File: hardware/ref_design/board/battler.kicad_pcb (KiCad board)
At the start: 2 copper layers, 73.4 x 151.6 mm, 171 parts, among them J1 TYPE-C-31-M-12, J2 53261-0271, J3 FH12-50S-0.5SH(55), J4 53261-0271, J5 SWD, J7 DEBUG PADS, Q1 2N7002, Q3 2N7002, Q5 AO3400A, Q6 AO3400A, Q7 2N7002, SW1 P1 UP, SW10 P2 DOWN, SW11 P2 LEFT, SW12 P2 RIGHT, SW13 P2 A, SW14 P2 B, SW15 P2 X, SW16 P2 Y, SW18 BOOTSEL, SW19 RESET, SW2 P1 DOWN, SW20 P1 SELECT, SW21 P1 START / PWR, SW22 P2 SELECT, SW23 P2 START / PWR, SW3 P1 LEFT, SW4 P1 RIGHT, SW5 P1 A, SW6 P1 B, SW7 P1 X, SW8 P1 Y, SW9 P2 UP, U1 SRV05-4, U2 BQ24073RGTR, U3 RT9013-33GB, U4 RP2354B, U6 MCP6002, U7 FM8002A, U8 SN74HC165PWR, U9 SN74HC165PWR, X1 12MHz

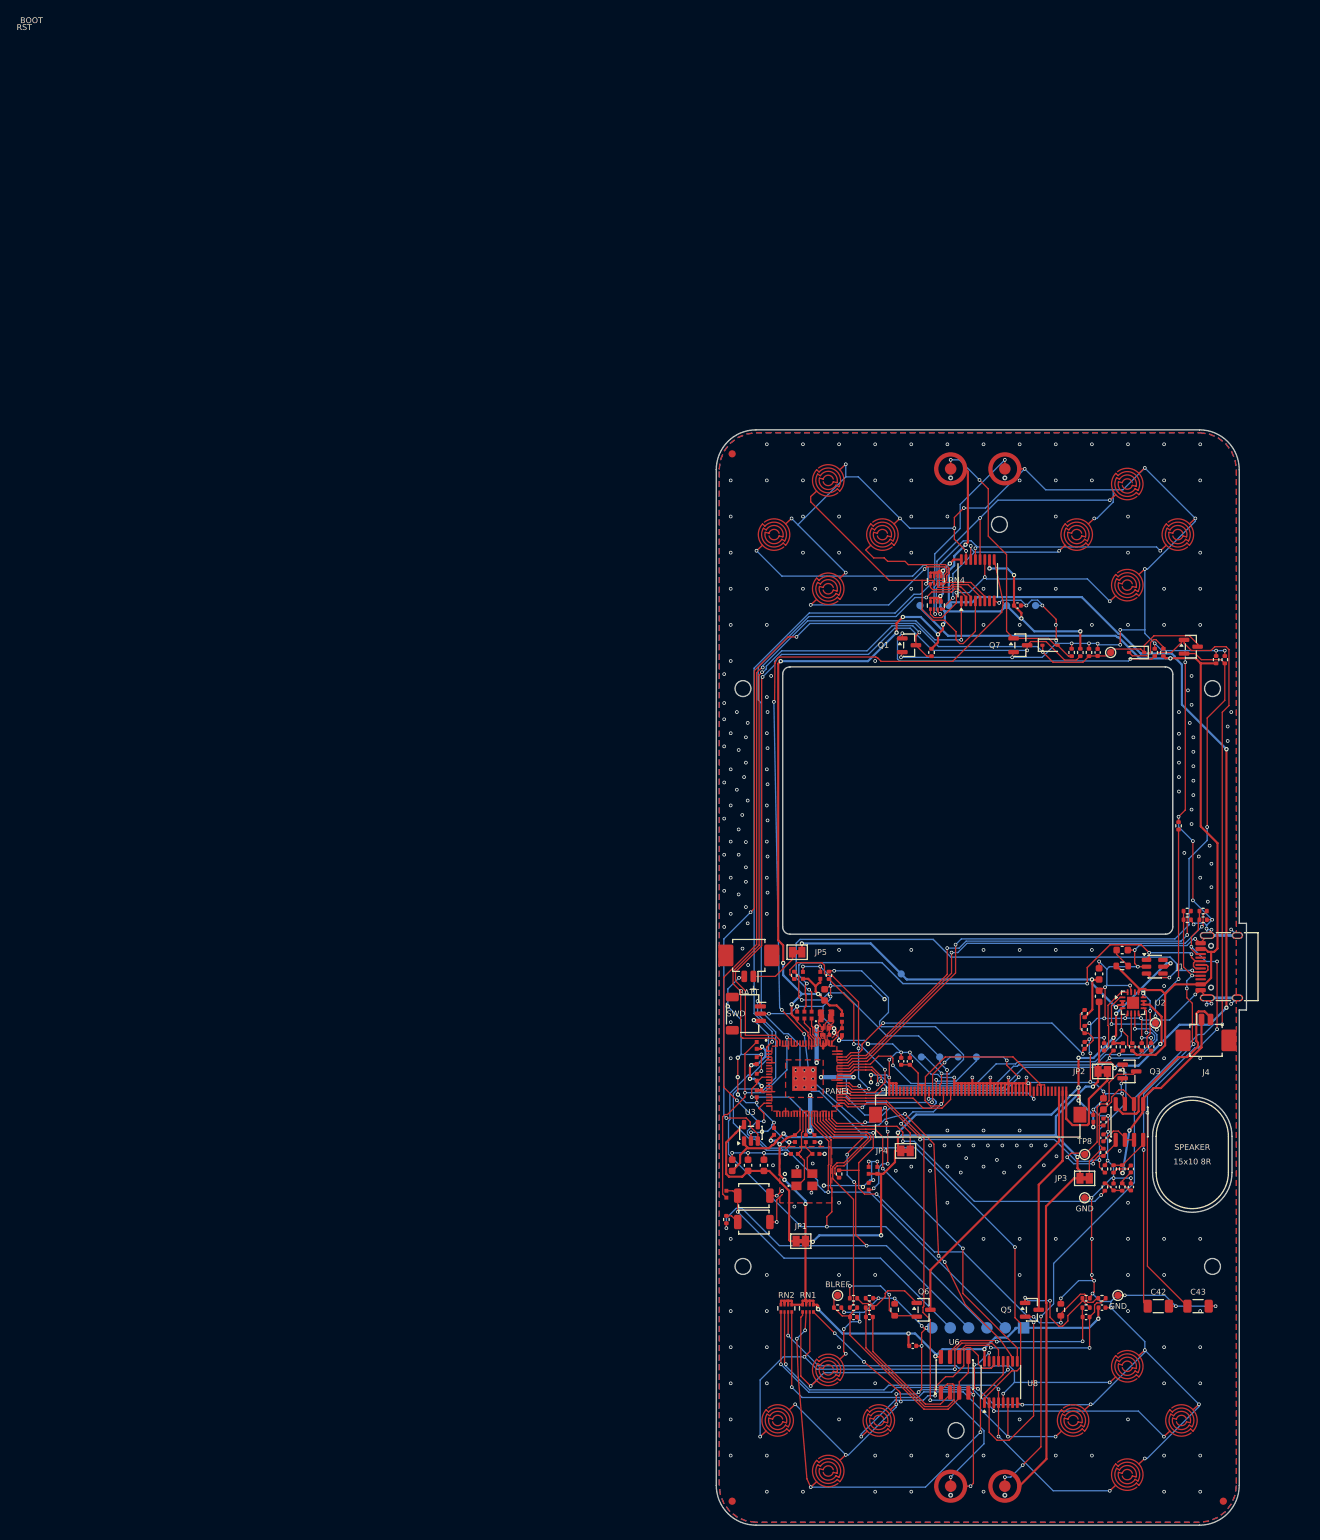
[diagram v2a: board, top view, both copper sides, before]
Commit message: ref_design: routed board for the turned cell hole (0 DRC errors, 2 connections still open: PWR_BTN_RAW and J3 pad 8's GND link), silk name on the back clear of holes, J2 nudged 0.15 in, Q1 0.15 up, pour edge clearance 0.31, docs for the V&V round 3 parts
Co-Authored-By: Claude Sonnet 5.5 <noreply@anthropic.com>
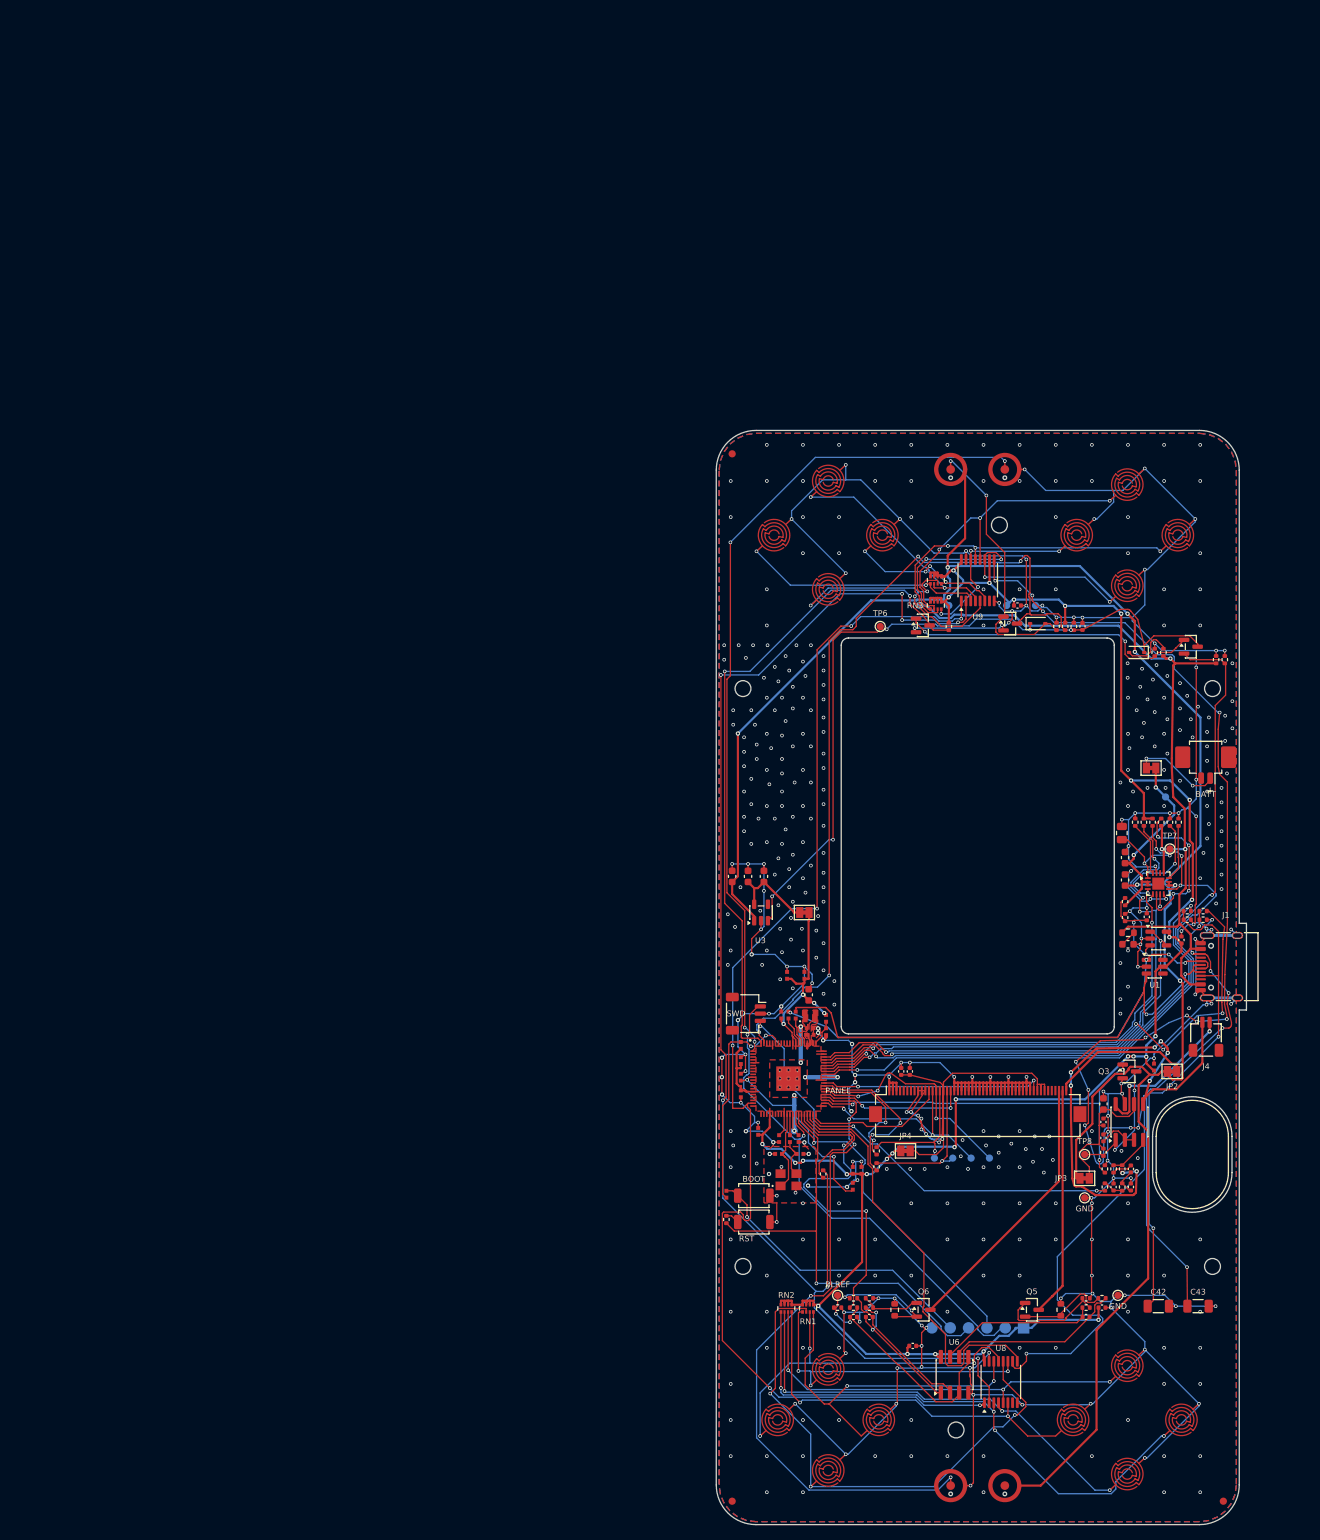
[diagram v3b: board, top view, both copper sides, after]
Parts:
- added C54: 100n, Capacitor_SMD:C_0402_1005Metric, F.Cu at (128.2, 94.8)
- added U10: MCP6001, Package_TO_SOT_SMD:SOT-23-5, F.Cu at (125.0, 94.6)
- J4: value 53261-0271 -> SM02B-SRSS-TB; footprint Connector_Molex:Molex_PicoBlade_53261-0271_1x02-1MP_P1.25mm_Horizontal -> Connector_JST:JST_SH_SM02B-SRSS-TB_1x02-1MP_P1.00mm_Horizontal
- R14, RN1, RN2, RN3, RN4: value 10k -> 47k
- R43: value 100k -> 220k
- R61: value 3.9k -> 3.74k
- TH1: value 10k B3950 -> 10k B4460; footprint Resistor_SMD:R_0402_1005Metric -> Resistor_SMD:R_0805_2012Metric
- moved J2 68.9 mm to (131.5, 70.0)
- moved JP5 55.2 mm to (124.0, 71.0)
- moved JP1 45.5 mm to (76.0, 91.0)
- moved TP3 44.0 mm to (126.0, 75.0)
- moved C5 40.0 mm to (66.0, 86.0)
- moved C6 40.0 mm to (68.2, 86.0)
- moved C7 40.0 mm to (70.4, 86.0)
- moved TP6 32.1 mm to (86.5, 51.4)
- moved R5 31.4 mm to (121.8, 78.5)
- moved R9 31.4 mm to (123.0, 78.5)
- moved R10 31.4 mm to (124.2, 78.5)
- moved R43 31.4 mm to (125.4, 78.5)
- moved R44 31.3 mm to (126.6, 78.5)
- moved R64 31.3 mm to (127.8, 78.5)
- moved U3 30.5 mm to (70.0, 91.0)
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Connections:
- C8 pad 1: VBAT_SENSE -> /Power/VBAT_DIV
- R17 pad 2: VBAT_SENSE -> /Power/VBAT_DIV
- R18 pad 1: VBAT_SENSE -> /Power/VBAT_DIV
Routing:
- net PWR_BTN_RAW: track 183.4 -> 41.7 mm, vias 6 -> 2
- net /Audio/SPK_P: track 26.0 -> 70.4 mm, vias 2 -> 8
- net /Buttons/SR_CHAIN: track 157.0 -> 197.1 mm, vias 6 -> 14
- net /Power/PWR_EN: track 141.1 -> 103.3 mm, vias 4 -> 5
- net CHG_STAT_N: track 55.4 -> 91.0 mm, vias 3 -> 4
- net VBAT: track 57.0 -> 26.4 mm, vias 3 -> 2
- net CHG_PG_N: track 56.0 -> 84.5 mm, vias 3 -> 5
- net CHG_OFF: track 53.1 -> 81.3 mm, vias 2 -> 4
- net /USB_Charger/CHG_TEMP: track 40.2 -> 12.1 mm, vias 4 -> 2
- net VSYS: track 260.5 -> 288.3 mm, vias 8 -> 7
- net /Display/LCD_3V3: track 48.6 -> 75.3 mm, vias 2 -> 8
- net P1_SELECT: track 69.5 -> 91.5 mm, vias 2 -> 4
- net SWDIO: track 85.6 -> 63.9 mm
- net /Display/LCD_SCK: track 38.3 -> 18.0 mm, vias 2 -> 1
- net +3V3: track 358.6 -> 340.8 mm, vias 38 -> 32
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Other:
- board size 73.4 x 151.6 mm -> 73.4 x 151.5 mm
- board text removed: "15x10 8R"
- board text removed: "SPEAKER"

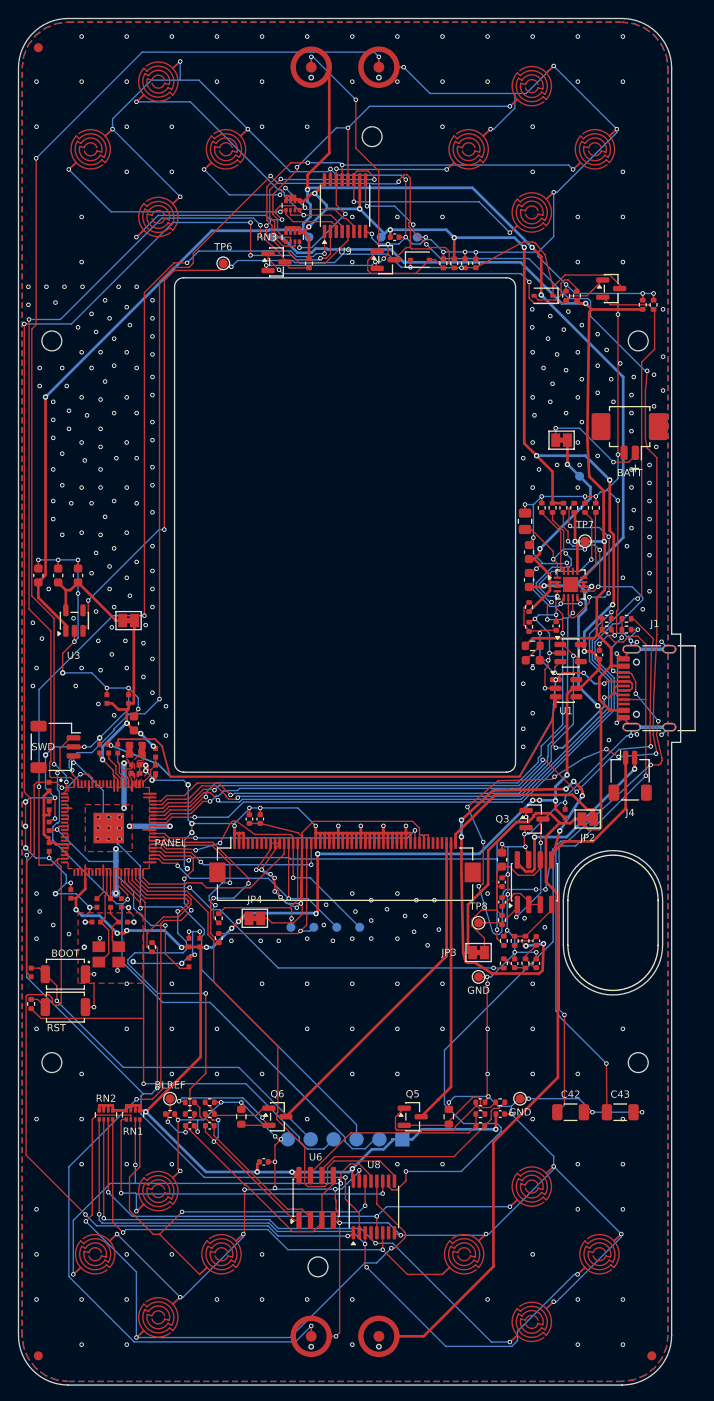
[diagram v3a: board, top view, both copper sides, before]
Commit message: ref_design: cell hole 1 mm towards seat 2 (case.scad cell_dy 1, J2 0.3 up), the latch and the seat-2 Start's row placed again, routed board with 0 unconnected and 0 DRC errors (place_search.py route, seed 32 of 20 to 55, 5627 mm); check_pcb, check_fit and the case checks pass
Co-Authored-By: Claude Sonnet 5.5 <noreply@anthropic.com>
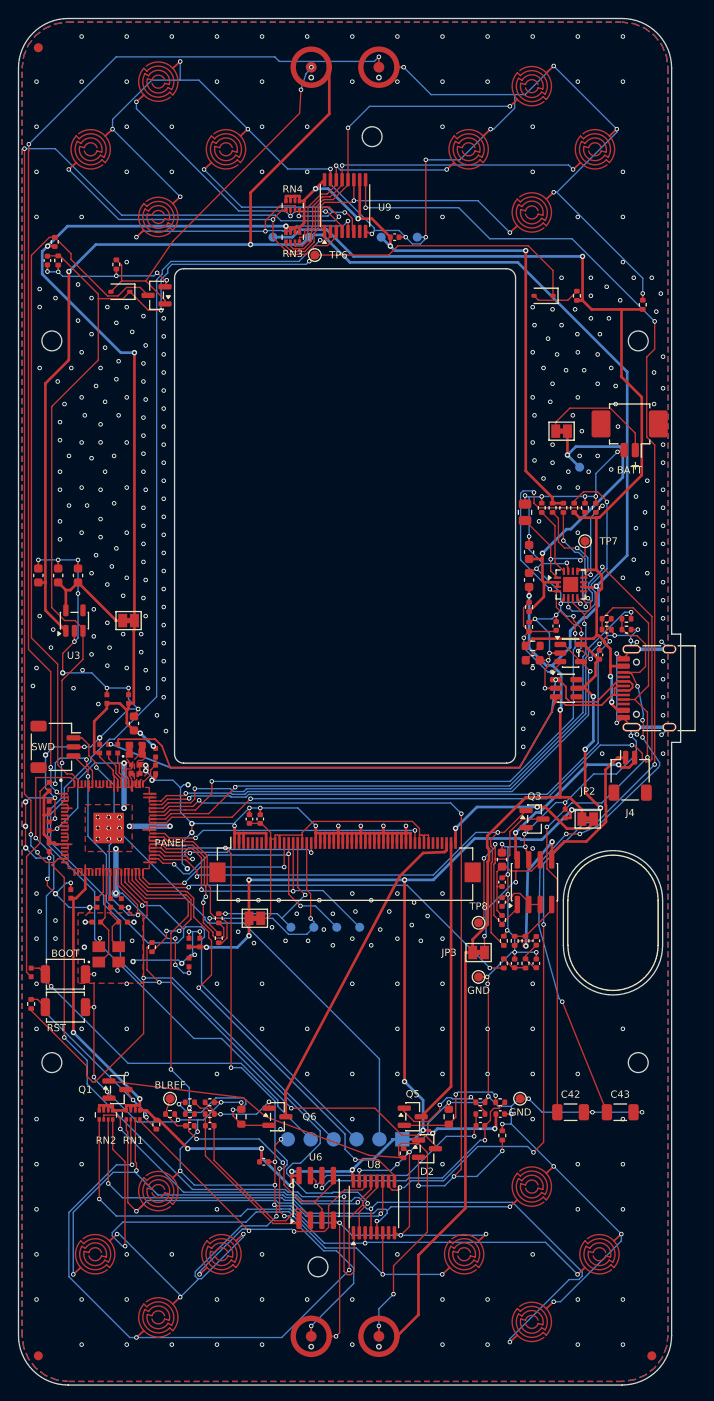
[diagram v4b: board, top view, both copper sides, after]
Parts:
- moved D2 97.5 mm to (109.1, 149.5)
- moved R16 97.0 mm to (79.1, 146.9)
- moved R13 96.7 mm to (106.5, 150.0)
- moved R42 93.6 mm to (117.4, 148.1)
- moved Q1 93.4 mm to (74.8, 143.0)
- moved C47 47.5 mm to (67.0, 51.1), turned to -90 degrees
- moved R15 45.1 mm to (68.2, 51.1), turned to -90 degrees
- moved R63 44.3 mm to (67.8, 49.0), turned to -90 degrees
- moved R62 36.3 mm to (74.6, 51.5), turned to -90 degrees
- moved D8 33.4 mm to (75.1, 54.5), turned to 180 degrees
- moved Q7 25.7 mm to (79.1, 54.9), turned to 180 degrees
- moved TP6 10.2 mm to (96.6, 50.5), turned to 180 degrees
- moved JP5 1.00 mm to (124.0, 70.0)
- moved TH1 1.00 mm to (120.0, 79.0)
- moved TP3 1.00 mm to (126.0, 74.0)
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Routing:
- net /Power/PWR_EN: track 103.3 -> 195.4 mm, vias 5 -> 4
- net +3V3: track 340.8 -> 406.7 mm, vias 32 -> 28
- net PWR_BTN_N: track 93.8 -> 53.4 mm, vias 2 -> 3
- net /Audio/SPK_P: track 70.4 -> 31.3 mm, vias 8 -> 2
- net /Buttons/SR_CHAIN: track 197.1 -> 158.7 mm, vias 14 -> 6
- net /Display/LCD_3V3: track 75.3 -> 38.0 mm, vias 8 -> 0
- net P2_START: track 113.4 -> 78.7 mm, vias 4 -> 0
- net /Buttons/SR_CLK: track 189.3 -> 162.0 mm, vias 7 -> 3
- net SR_PL: track 177.0 -> 199.7 mm
- net PWR_BTN_RAW: track 41.7 -> 62.6 mm
- net PWR_HOLD: track 110.9 -> 91.1 mm, vias 2 -> 5
- net P1_SELECT: track 91.5 -> 75.5 mm, vias 4 -> 6
- net VSYS: track 288.3 -> 273.5 mm, vias 7 -> 5
- net /Buttons/P1_B: track 64.1 -> 78.0 mm
- net BL_PWM: track 46.6 -> 34.0 mm
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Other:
- outline, holes or cut-outs redrawn
